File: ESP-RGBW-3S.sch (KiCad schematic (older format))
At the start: 34 parts, among them J1 12V IN, J2 PROG, J3 LED Str., J4 Temp. S., J5 Light. S., J6 PIR, Q1 IRLML0040TRPBF, Q2 IRLML0040TRPBF, Q3 IRLML0040TRPBF, Q4 IRLML0040TRPBF, SW1 Flash, U2 ESP-12E, U4 DCDC_LM2596

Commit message: v 0.2
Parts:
- C1, C2: footprint Capacitor_SMD:C_0805_2012Metric_Pad1.15x1.40mm_HandSolder -> Capacitor_SMD:C_0805_2012Metric
- Q1, Q2, Q3, Q4: footprint Package_TO_SOT_SMD:SOT-23_Handsoldering -> Package_TO_SOT_SMD:SOT-23
- R1, R10, R11, R12, R13, R14, R15, R16, R17, R18, R2, R3, R4, R5, R6, R7, R8, R9: footprint Resistor_SMD:R_0805_2012Metric_Pad1.20x1.40mm_HandSolder -> Resistor_SMD:R_0805_2012Metric
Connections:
- net B-Out: now also Q2.3 (D); no longer Q3.3 (D)
- net Blue: now also R13.1, U2.6 (GPIO12); no longer R12.1, U2.5 (GPIO14)
- net G-Out: now also Q4.3 (D); no longer Q1.3 (D)
- net R-Out: now also Q3.3 (D); no longer Q2.3 (D)
- net Red: now also R12.1, U2.5 (GPIO14); no longer R13.1, U2.6 (GPIO12)
- net W-Out: now also Q1.3 (D); no longer Q4.3 (D)
- net Green renamed White
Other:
- moved on the sheet: Q1, Q2, Q3, Q4, R11, R12, R13, R14, R15, R16, R17, R18

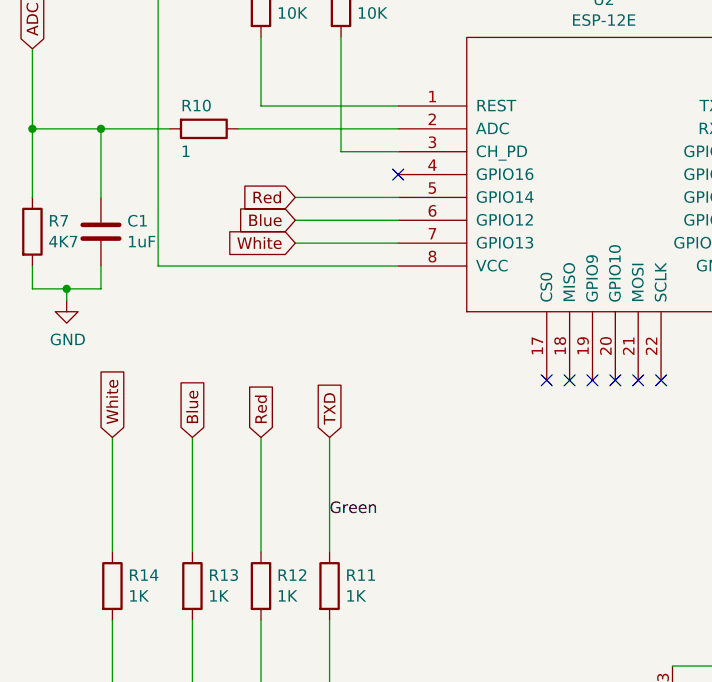
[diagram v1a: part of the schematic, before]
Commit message: GPIO15 as Red ch. output instead of TX
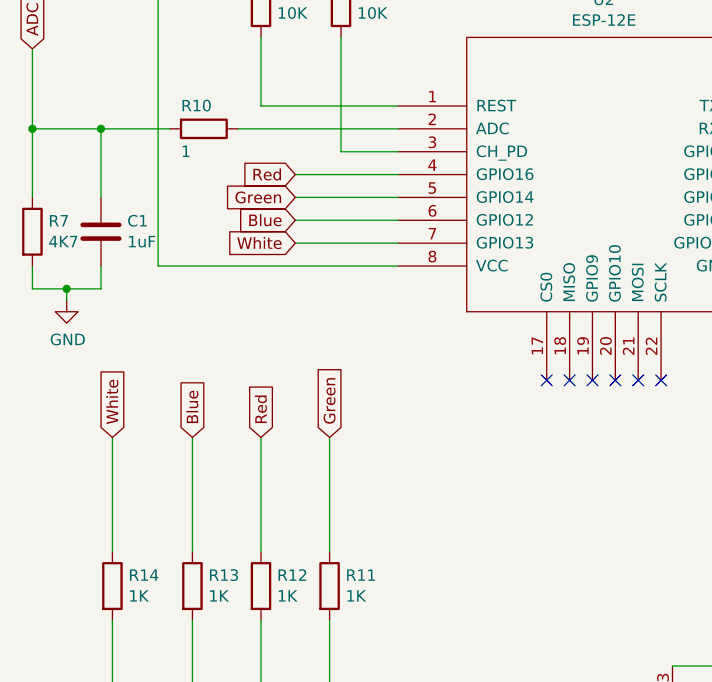
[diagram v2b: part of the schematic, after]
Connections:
- net Red: now also U2.4 (GPIO16); no longer U2.5 (GPIO14)
- net TXD: no longer R11.1
- new net Green: R11.1, U2.5 (GPIO14)
- no-connect marks 12 -> 11
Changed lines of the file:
@@
 $EndComp
 Text GLabel 2000 3000 1    50   Input ~ 0
-TXD
+Green
 Text GLabel 1050 3000 1    50   Input ~ 0
 White
 Wire Wire Line
 	2000 3000 2000 3500
-Text Label 2000 3350 0    50   ~ 0
-Green
 Text GLabel 1700 3000 1    50   Input ~ 0
 Red
@@
 Wire Wire Line
 	2300 1950 1850 1950
+Text GLabel 1850 1850 0    50   Input ~ 0
+Red
 Text GLabel 1850 1950 0    50   Input ~ 0
-Red
-NoConn ~ 2300 1850
+Green
+Wire Wire Line
+	2300 1850 1850 1850
 $EndSCHEMATC

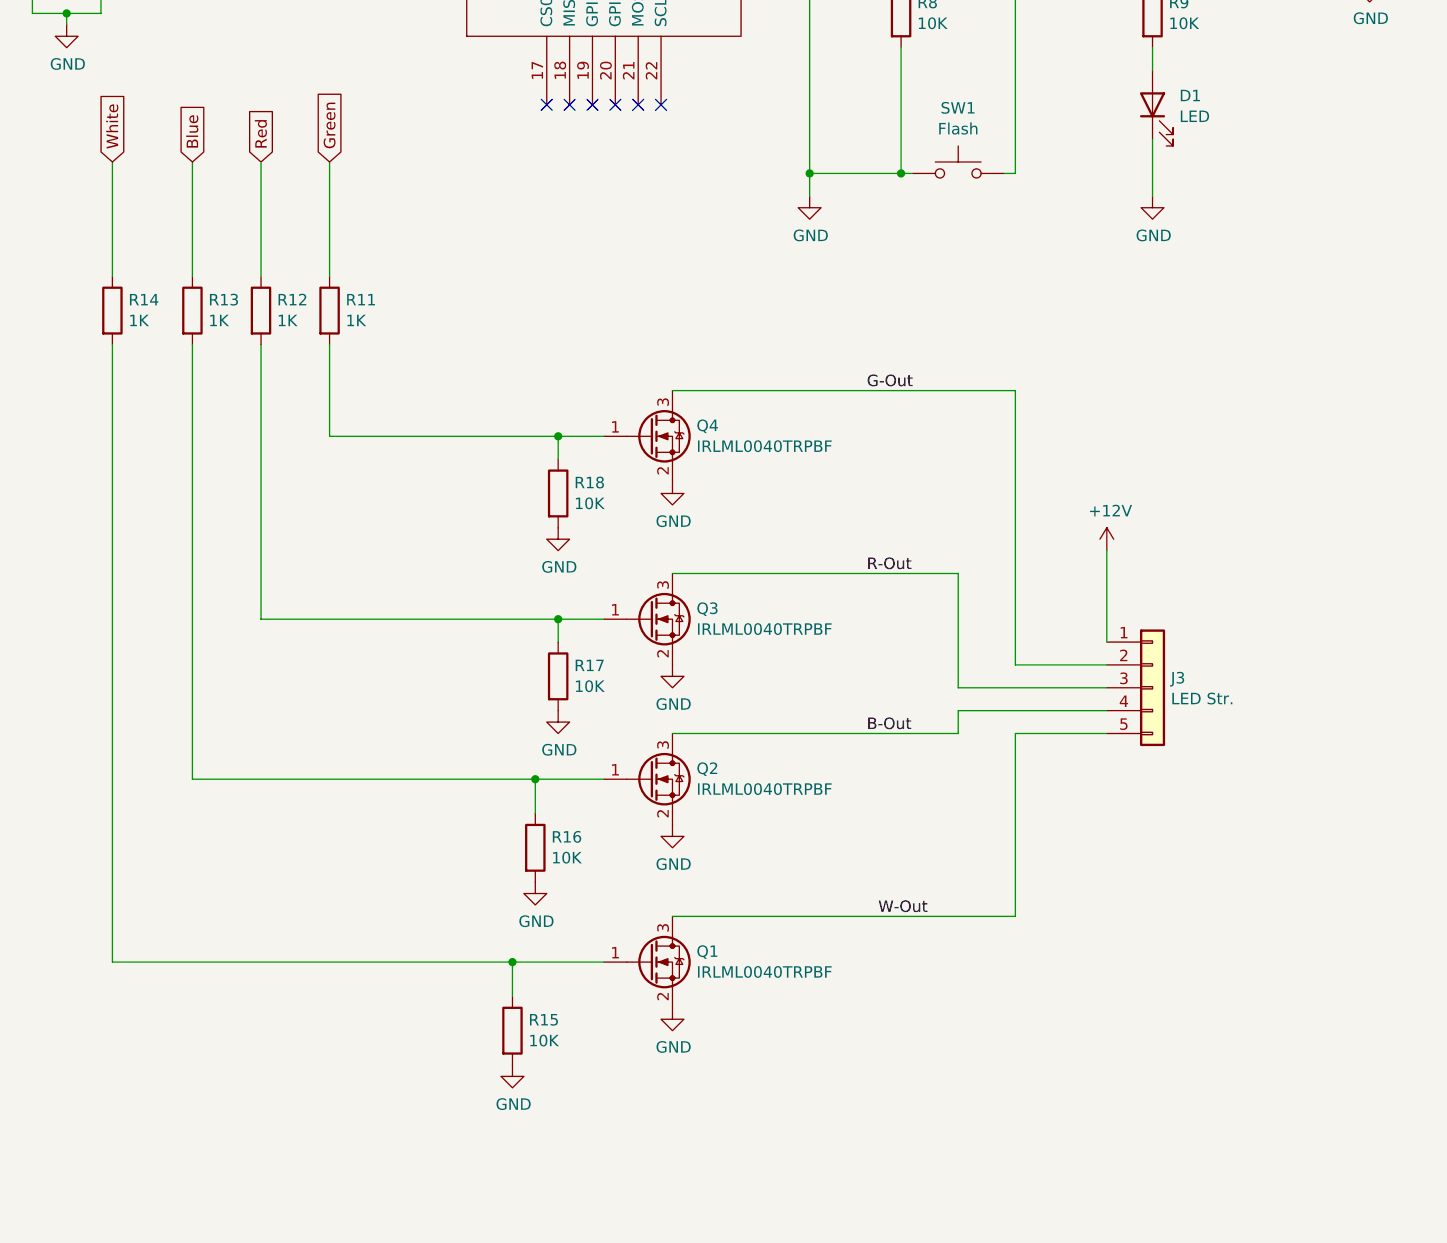
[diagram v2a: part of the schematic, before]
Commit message: v 0.4, pull-up option for GPIO 12-14
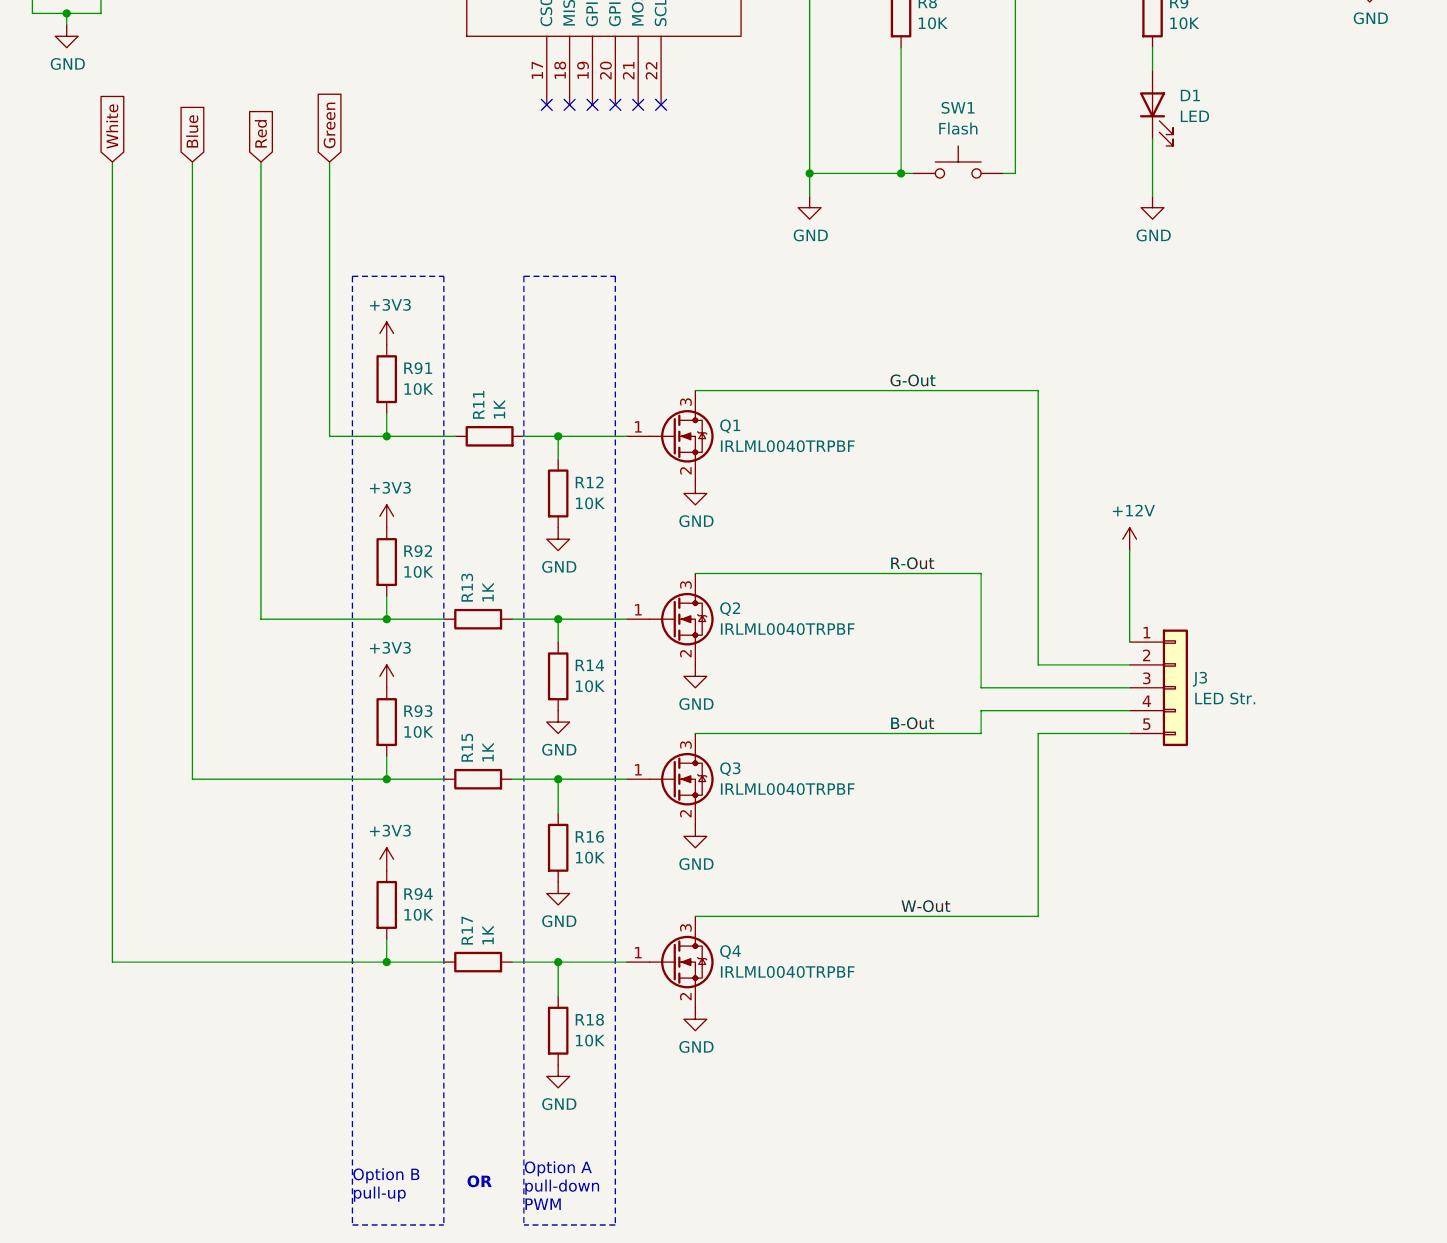
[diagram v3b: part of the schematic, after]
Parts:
- added R91, R92, R93, R94: 10K, Resistor_SMD:R_0805_2012Metric, symbol Device:R
- renumbered Q4 to Q1, Q3 to Q2, Q2 to Q3, Q1 to Q4, R18 to R12, R12 to R13, R17 to R14, R13 to R15, R14 to R17, R15 to R18
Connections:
- net +3V3: now also R91.1, R92.1, R93.1, R94.1
- net Blue: now also R93.2
- net Green: now also R91.2
- net Red: now also R92.2
- net White: now also R94.2
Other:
- note added: "OR"
- note added: "Option A\npull-down\nPWM"
- note added: "Option B\npull-up"
- moved on the sheet: J3, Q1, Q2, Q3, Q4, R11, R13, R15, R16, R17, R18

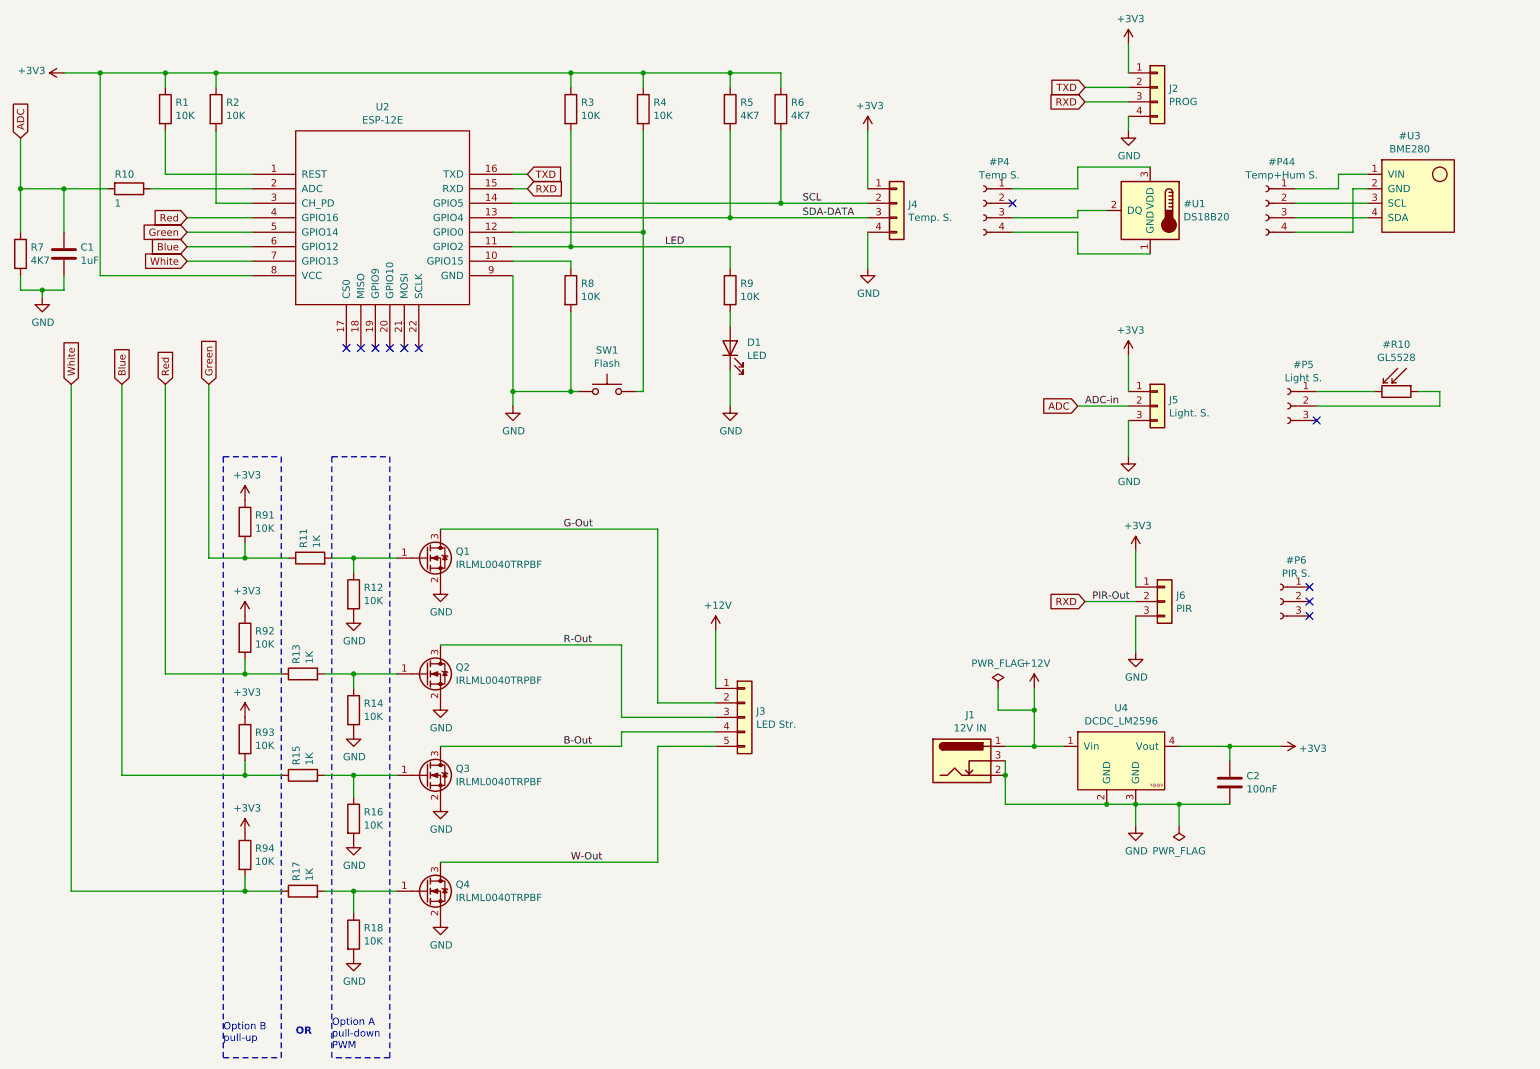
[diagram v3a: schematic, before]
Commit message: optional pull-up and pull-down resistors for TX-RX
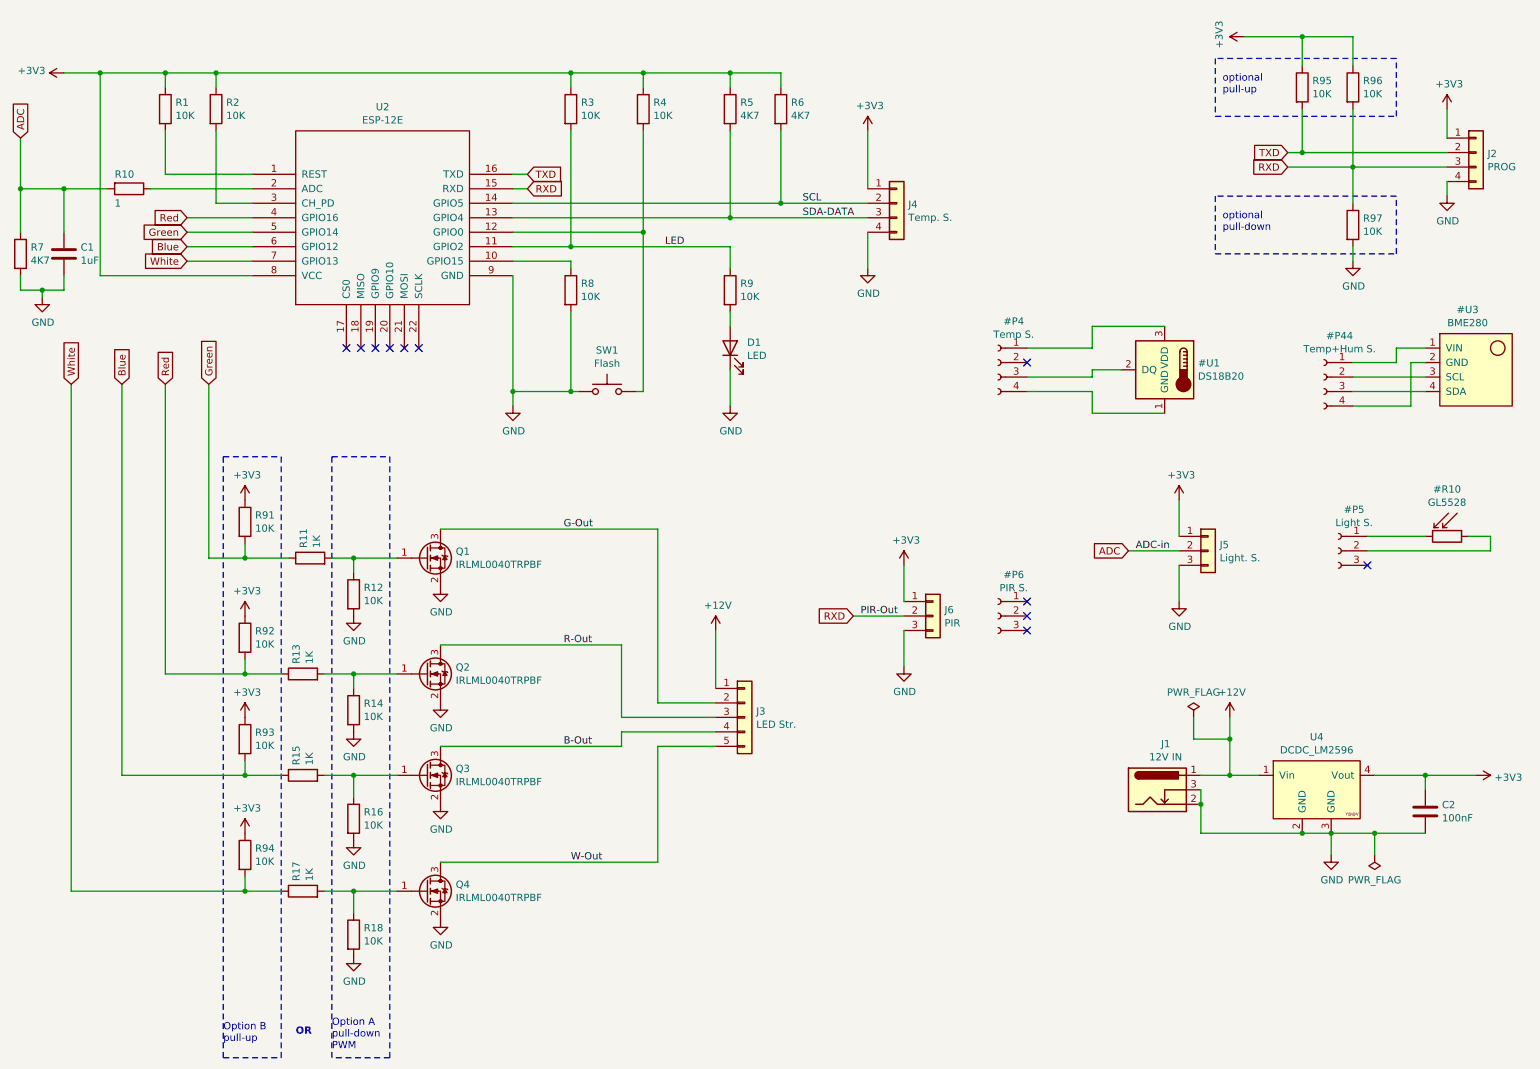
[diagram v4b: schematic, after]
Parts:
- added R95, R96, R97: 10K, Resistor_SMD:R_0805_2012Metric, symbol Device:R
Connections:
- net +3V3: now also R95.1, R96.1
- net GND: now also R97.2
- net RXD: now also R96.2, R97.1
- net TXD: now also R95.2
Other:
- note added: "optional\npull-down"
- note added: "optional\npull-up"
- moved on the sheet: C2, J1, J2, J5, J6, U4
